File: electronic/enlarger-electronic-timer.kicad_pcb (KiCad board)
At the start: 2 copper layers, 50 x 52 mm, 16 parts, among them J1 RELAY, J2 DIGIT, J3 FORCE, J4 INCREASE, J5 DECREASE, J6 TIMER, J7 USB_OTG

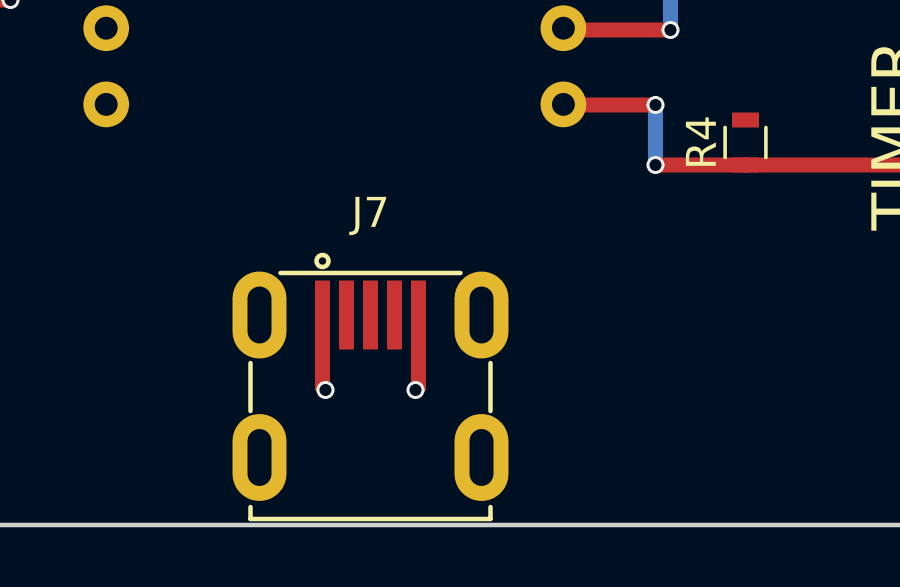
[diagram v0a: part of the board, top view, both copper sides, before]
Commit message: Added link between USB GND pin and GND holes.
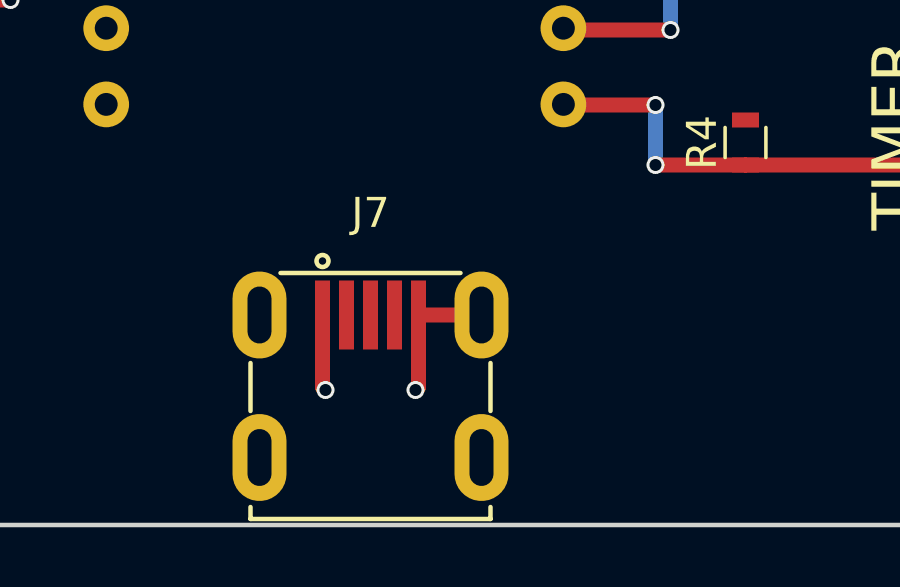
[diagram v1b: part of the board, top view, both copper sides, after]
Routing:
- net GND: track 2.54 -> 4.64 mm
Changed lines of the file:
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@@
     (links 29)
     (no_connects 0)
-    (area 49.924999 49.924999 100.075001 102.075001)
+    (area 30.364287 37.3 121.427507 103.875)
     (thickness 1.6)
     (drawings 16)
-    (tracks 56)
+    (tracks 57)
     (zones 0)
     (modules 16)
@@
   (layers
     (0 F.Cu signal)
-    (31 B.Cu signal hide)
+    (31 B.Cu signal)
     (32 B.Adhes user)
     (33 F.Adhes user)
@@
   (segment (start 73.4 97.4) (end 73.5 97.5) (width 0.5) (layer F.Cu) (net 23))
   (via (at 73.5 97.5) (size 0.6) (drill 0.4) (layers F.Cu B.Cu) (net 23))
+  (segment (start 76.6 95) (end 78.7 95) (width 0.5) (layer F.Cu) (net 24))
   (segment (start 76.6 95) (end 76.6 97.4) (width 0.5) (layer F.Cu) (net 24))
   (segment (start 76.6 97.4) (end 76.5 97.5) (width 0.5) (layer F.Cu) (net 24))
